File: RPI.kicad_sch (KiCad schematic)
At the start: 24 parts, among them J1 Conn_01x02_Male, J1 GPIO, J2 Conn_02x12, J4 Conn_01x03, Q1 IRF9540N, U1 LM1085-5.0, U2 CAT24C256

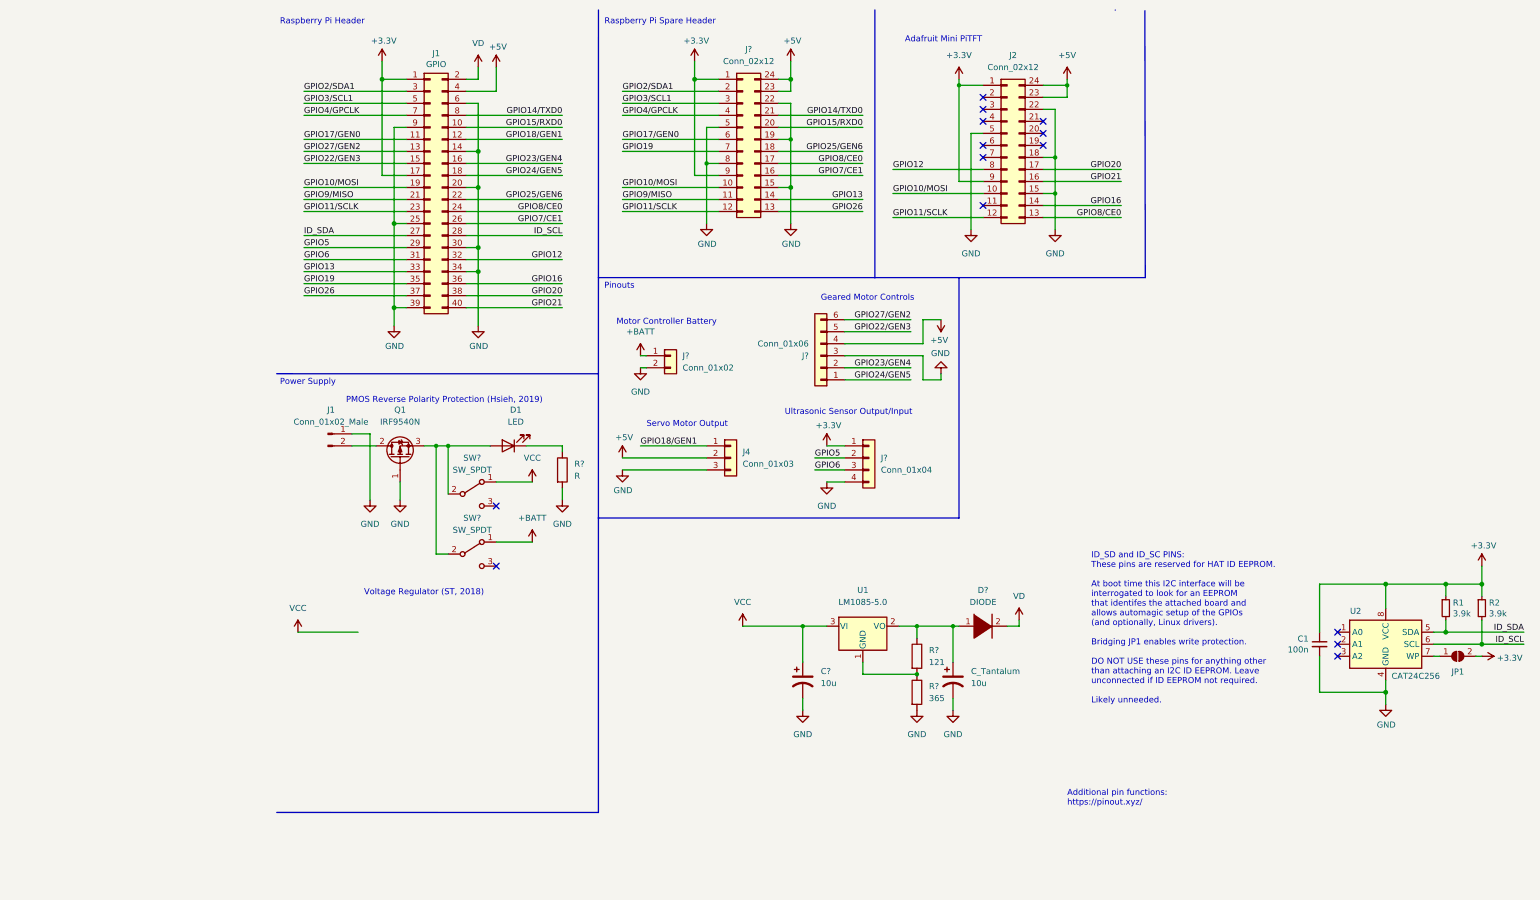
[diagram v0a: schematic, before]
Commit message: Removed EEPROM, Added back power protection
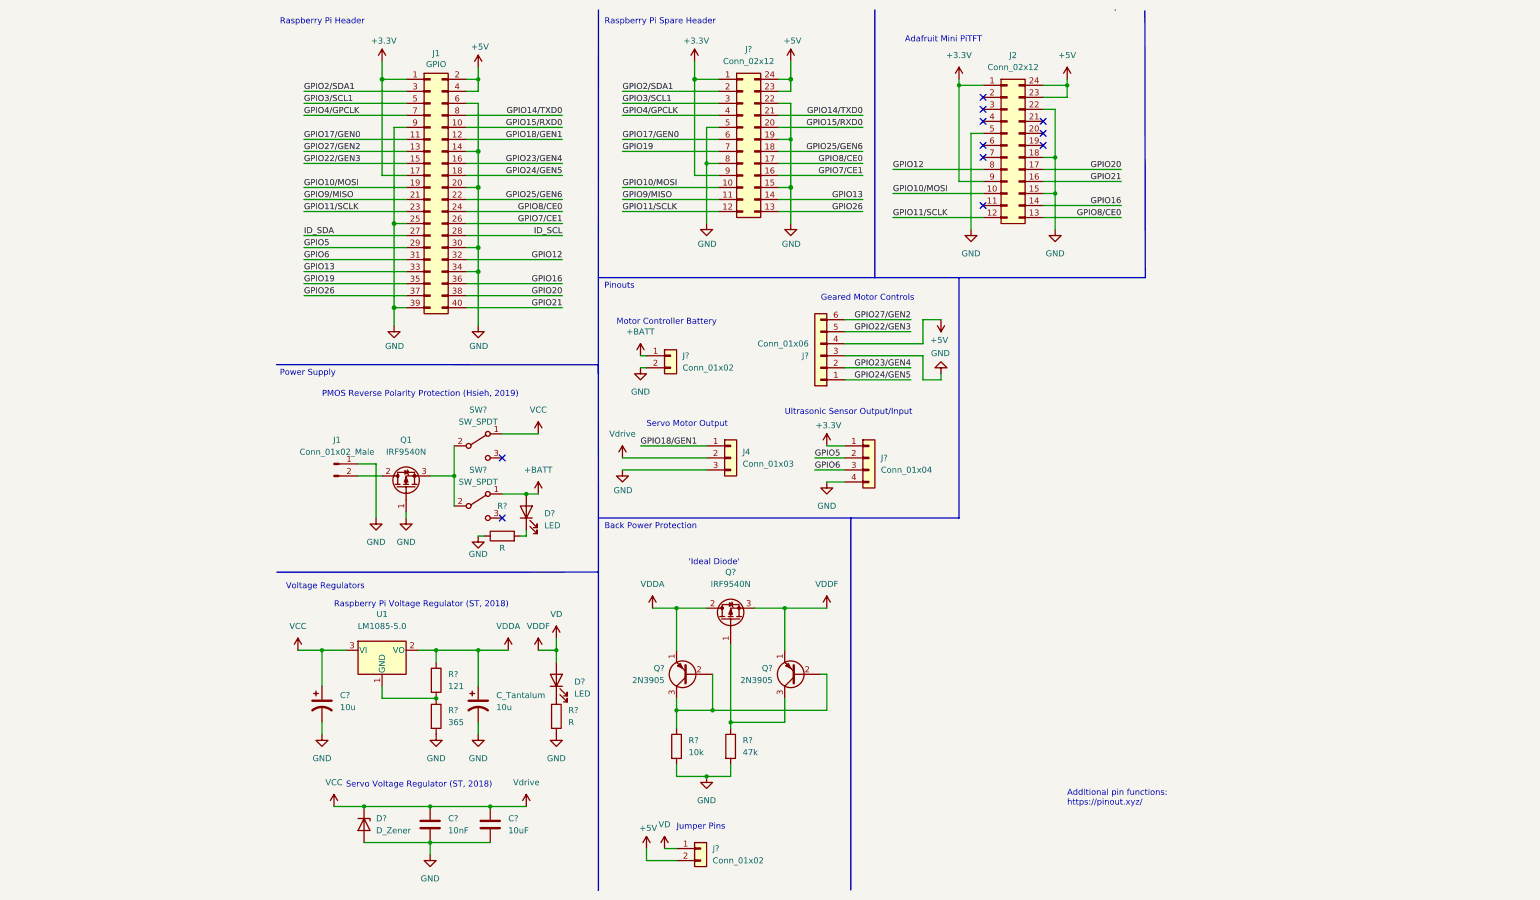
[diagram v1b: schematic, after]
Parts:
- removed C1: 100n, symbol Device:C_Small
- removed D1: LED, symbol Device:LED
- removed D?: DIODE, symbol pspice:DIODE
- removed JP1: ID_WP, symbol Jumper:SolderJumper_2_Open
- removed R1, R2: 3.9k, symbol Device:R_Small
- removed R?: R, symbol Device:R
- removed U2: CAT24C256, symbol Memory_EEPROM:CAT24C256
- added C?: 10uF, symbol Device:C
- added C?: 10nF, symbol Device:C
- added D? (x2): LED, symbol Device:LED
- added D?: D_Zener, symbol Device:D_Zener
- added J?: Conn_01x02, symbol Connector_Generic:Conn_01x02
- added Q? (x2): 2N3905, Package_TO_SOT_THT:TO-92_Inline, symbol Transistor_BJT:2N3905
- added Q?: IRF9540N, Package_TO_SOT_THT:TO-220-3_Vertical, symbol Transistor_FET:IRF9540N
- added R? (x2): R, symbol Device:R
- added R?: 47k, symbol Device:R
- added R?: 10k, symbol Device:R
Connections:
- net +5V: now also J1.2 (Pin_2), J?.2 (Pin_2); no longer J4.2 (Pin_2)
- net +BATT: now also D?.2 (A)
- net GND: now also C?.2, C?.2, D?.2 (A), R?.1, R?.2, R?.2, R?.2
- net VCC: now also J4.2 (Pin_2), C?.1, C?.1, D?.1 (K)
- net VD: now also D?.2 (A), J?.1 (Pin_1), Q?.1 (E), Q?.3 (S); no longer J1.2 (Pin_2)
- net VDDA: now reaches C_Tantalum.1, R?.1, U1.2 (VO)
- net VDDA: now also Q?.1 (E), Q?.2 (D)
- new net: D?.1 (K), R?.1
- new net: Q?.2 (B), Q?.2 (B), Q?.3 (C), R?.1
- new net: D?.1 (K), R?.2
- new net: Q?.1 (G), Q?.3 (C), R?.1
- no-connect marks 14 -> 11
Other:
- note added: "'Ideal Diode'"
- note added: "Back Power Protection"
- note added: "Jumper Pins"
- note added: "Raspberry Pi Voltage Regulator (ST, 2018)"
- note added: "Servo Voltage Regulator (ST, 2018)"
- note added: "Voltage Regulators"
- note removed: "ID_SD and ID_SC PINS: These pins are reserved for HAT ID EEPROM. At boot time this I2C interface will be interrogated to look for an EEPROM that identifes the attached board and allows automagic setup of the GPIOs (and optionally, Linux drivers). Bridging JP1 enables write protection. DO NOT USE these pins for anything other than attaching an I2C ID EEPROM. Leave unconnected if ID EEPROM not requ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"
- note removed: "Voltage Regulator (ST, 2018)"
- moved on the sheet: C?, C_Tantalum, J1, Q1, R?, SW?, U1

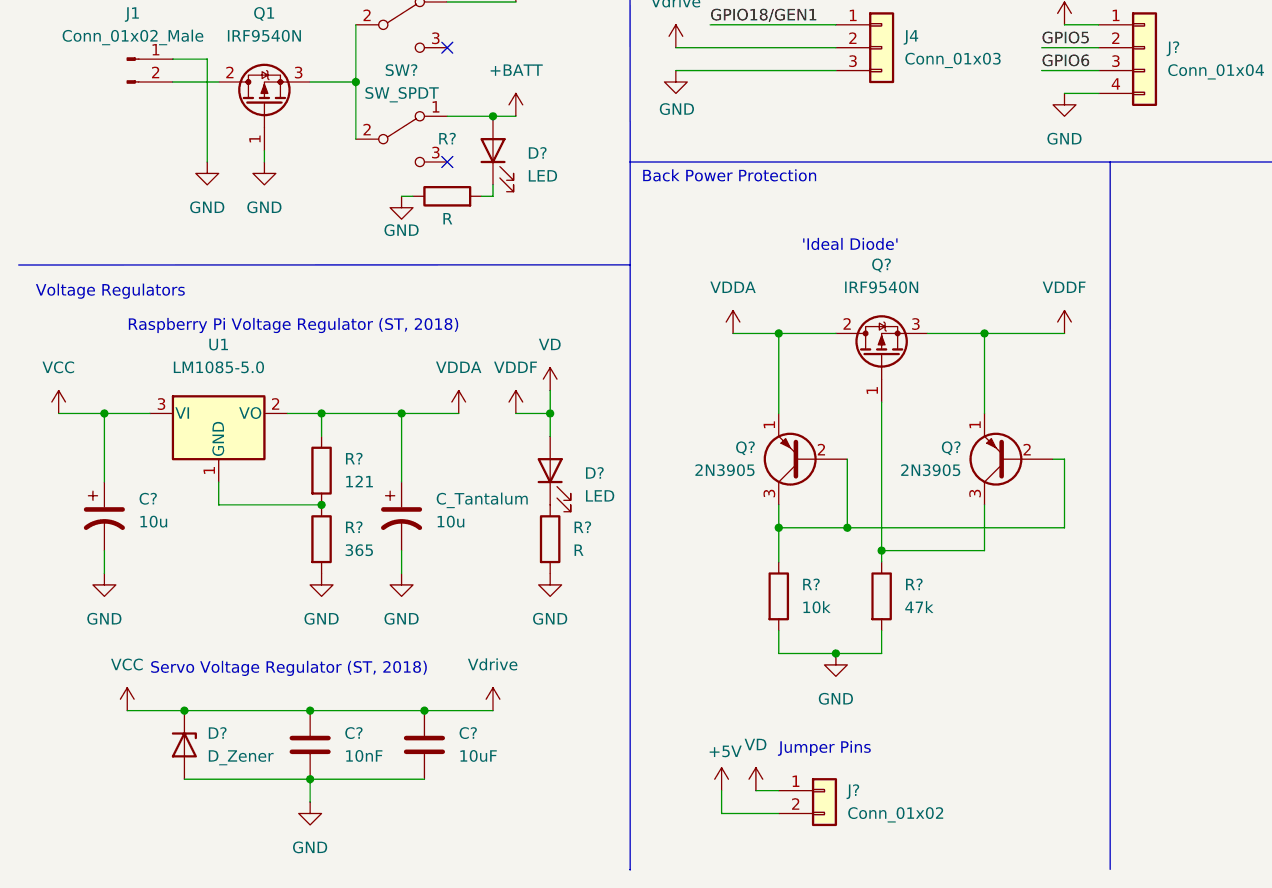
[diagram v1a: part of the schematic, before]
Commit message: Process to update headers for SMDs
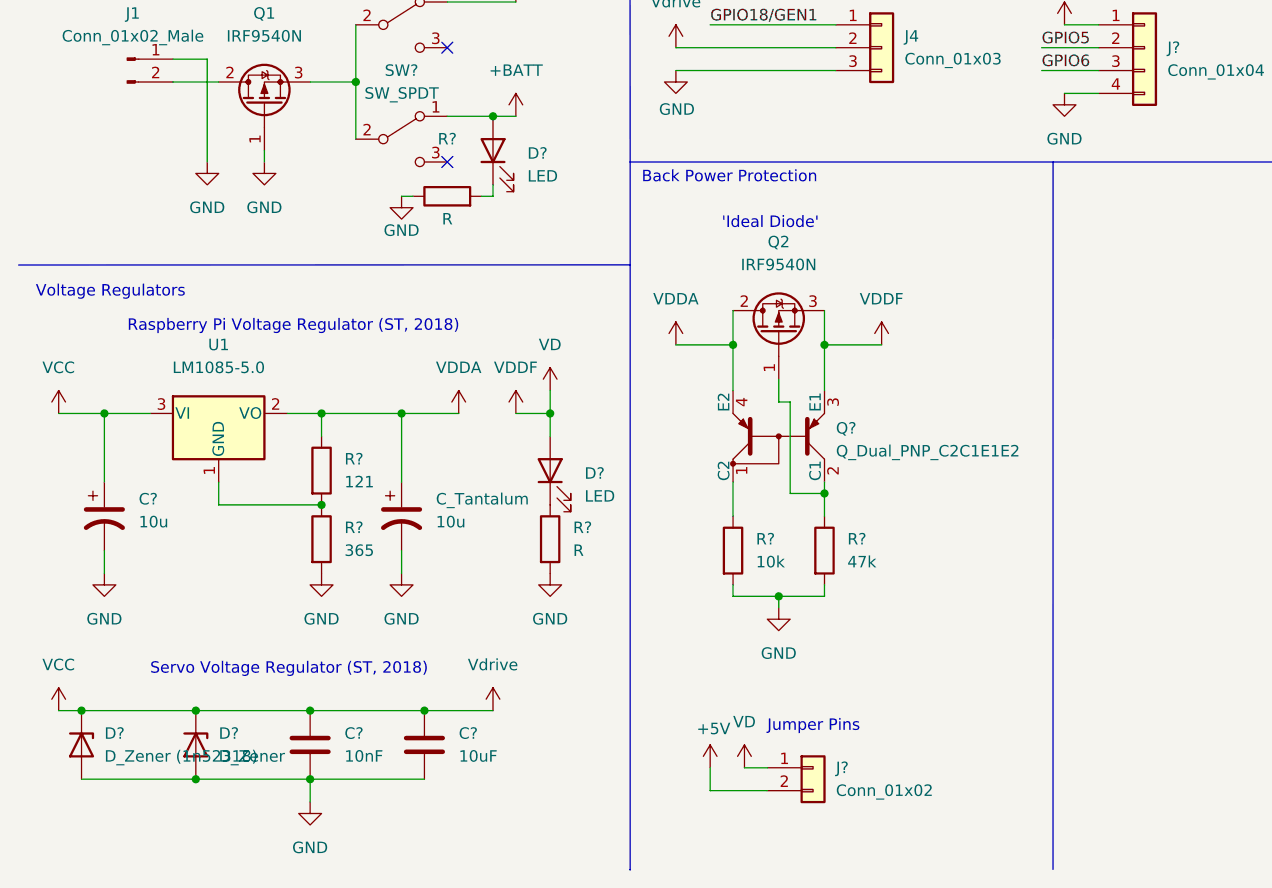
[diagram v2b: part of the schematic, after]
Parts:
- removed Q? (x2): 2N3905, Package_TO_SOT_THT:TO-92_Inline, symbol Transistor_BJT:2N3905
- removed Q?: IRF9540N, Package_TO_SOT_THT:TO-220-3_Vertical, symbol Transistor_FET:IRF9540N
- added D?: D_Zener (1n52318), symbol Device:D_Zener
- added Q2: IRF9540N, Package_TO_SOT_THT:TO-220-3_Vertical, symbol Transistor_FET:IRF9540N
- added Q?: Q_Dual_PNP_C2C1E1E2, symbol Device:Q_Dual_PNP_C2C1E1E2
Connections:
- net GND: now also D?.2 (A)
- net VCC: now also D?.1 (K)
- net VD: now also Q2.3 (S), Q?.3 (E1)
- net VDDA: now also Q2.2 (D), Q?.4 (E2)
- net at R?.1: now also Q?.1 (C2)
- net at R?.1: now also Q2.1 (G), Q?.2 (C1)
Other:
- moved on the sheet: D?, J?, R?

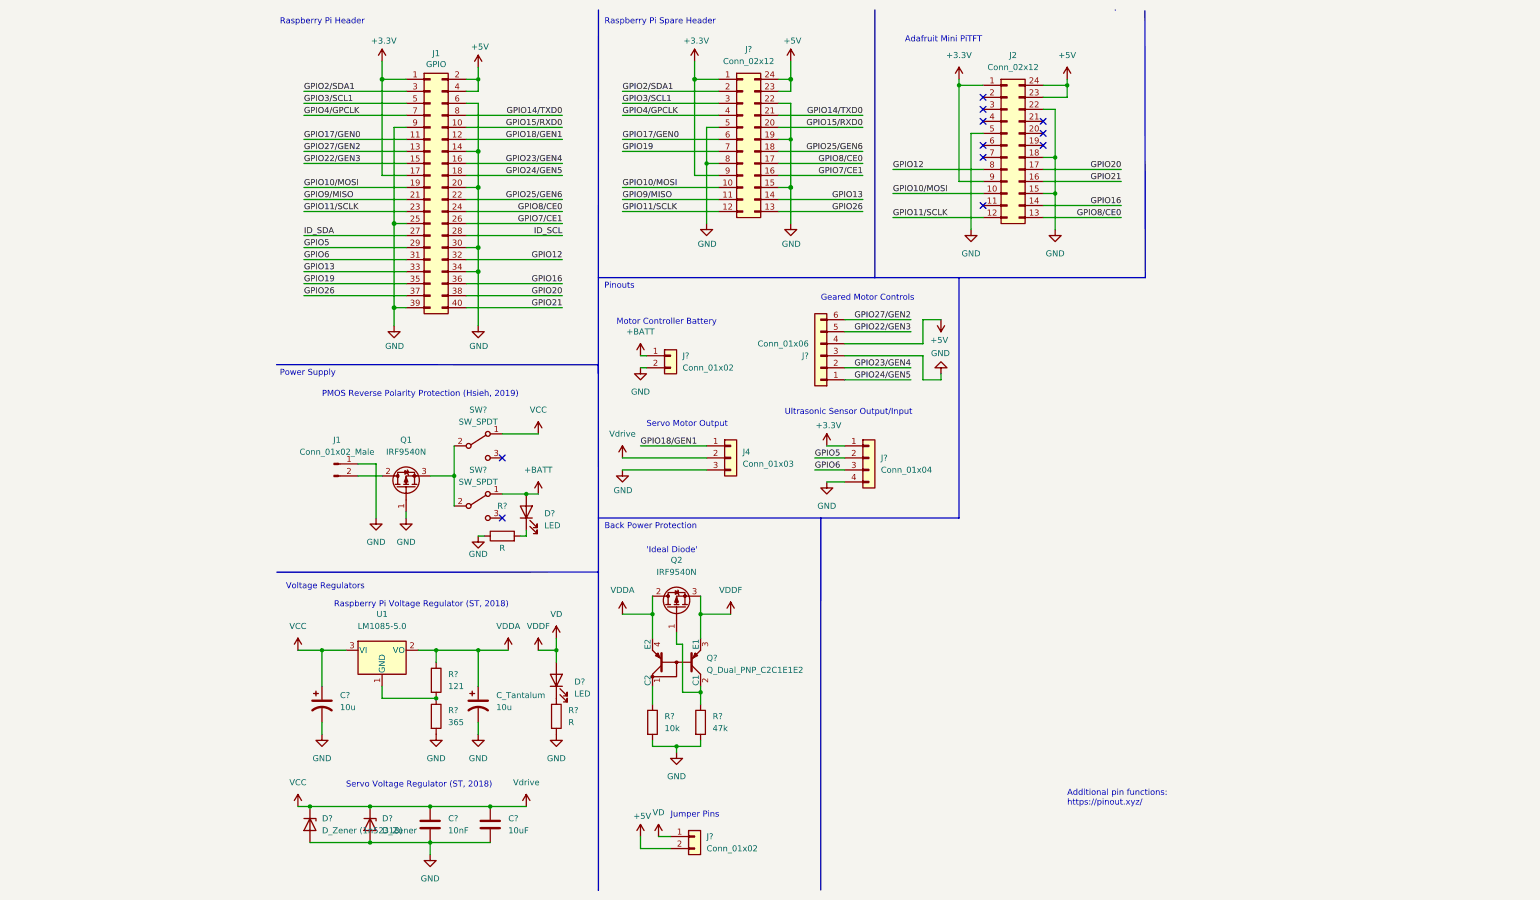
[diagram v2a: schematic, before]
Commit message: Component footprints done - only need cap & sw tbd
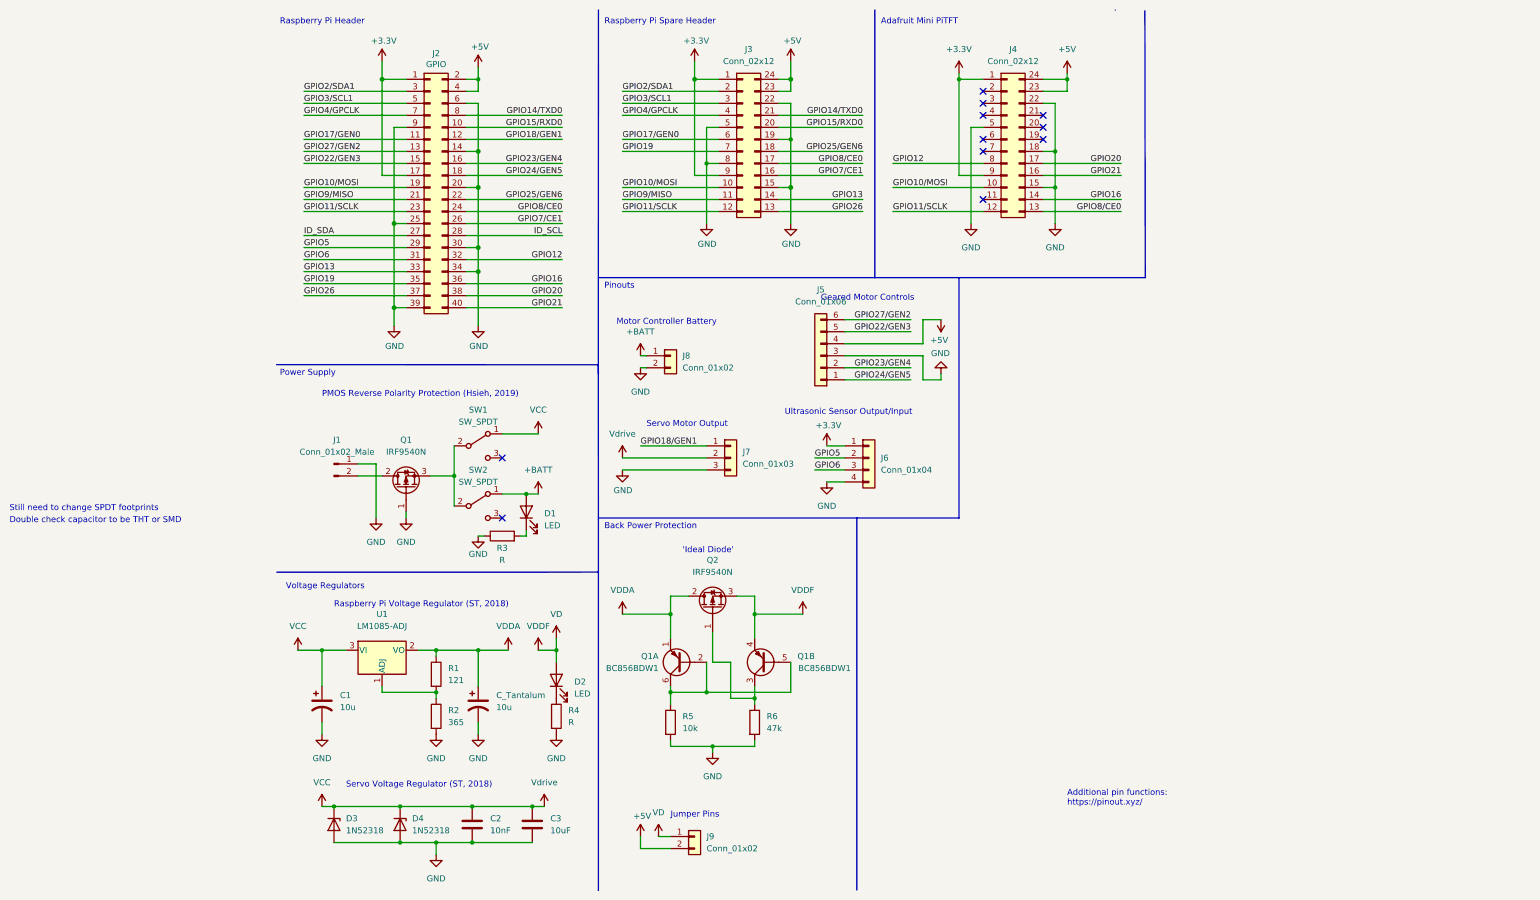
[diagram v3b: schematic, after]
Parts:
- removed D?: D_Zener, symbol Device:D_Zener
- removed Q?: Q_Dual_PNP_C2C1E1E2, symbol Device:Q_Dual_PNP_C2C1E1E2
- removed R? (x2): R, symbol Device:R
- removed R?: 121, symbol Device:R
- removed R?: 365, symbol Device:R
- removed R?: 47k, symbol Device:R
- removed R?: 10k, symbol Device:R
- removed U1: LM1085-5.0, symbol Regulator_Linear:LM1085-5.0
- added D4: 1N52318, Diode_THT:D_DO-35_SOD27_P7.62mm_Horizontal, symbol Device:D_Zener
- added Q1: BC856BDW1, Package_TO_SOT_SMD:SOT-363_SC-70-6, symbol Transistor_BJT:BC856BDW1
- added unit 2 of Q1
- added R1: 121, Resistor_SMD:R_0805_2012Metric_Pad1.20x1.40mm_HandSolder, symbol Device:R
- added R2: 365, Resistor_SMD:R_0805_2012Metric_Pad1.20x1.40mm_HandSolder, symbol Device:R
- added R3, R4: R, Resistor_SMD:R_0805_2012Metric_Pad1.20x1.40mm_HandSolder, symbol Device:R
- added R5: 10k, Resistor_SMD:R_0805_2012Metric_Pad1.20x1.40mm_HandSolder, symbol Device:R
- added R6: 47k, Resistor_SMD:R_0805_2012Metric_Pad1.20x1.40mm_HandSolder, symbol Device:R
- added U1: LM1085-ADJ, symbol Regulator_Linear:LM1085-ADJ
- D1, D2: renamed from D?; footprint (none) -> Diode_SMD:D_0805_2012Metric_Pad1.15x1.40mm_HandSolder
- D3: renamed from D?; value D_Zener (1n52318) -> 1N52318; footprint (none) -> Diode_THT:D_DO-35_SOD27_P7.62mm_Horizontal
- J3: renamed from J?; footprint (none) -> Connector_PinSocket_2.54mm:PinSocket_2x12_P2.54mm_Vertical
- J4: renamed from J2; footprint (none) -> Connector_PinSocket_2.54mm:PinSocket_2x12_P2.54mm_Vertical
- J5: renamed from J?; footprint (none) -> Connector_PinSocket_2.54mm:PinSocket_1x06_P2.54mm_Vertical
- J6: renamed from J?; footprint (none) -> Connector_PinSocket_2.54mm:PinSocket_1x04_P2.54mm_Vertical
- J7: renamed from J4; footprint (none) -> Connector_PinSocket_2.54mm:PinSocket_1x03_P2.54mm_Vertical
- J8, J9: renamed from J?; footprint (none) -> Connector_PinSocket_2.54mm:PinSocket_1x02_P2.54mm_Vertical
- gave numbers to parts that had none: 5
- renumbered J1 to J2
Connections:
- net GND: now also D4.2 (A), R2.2, R3.1, R4.2, R5.2, R6.2
- net VCC: now also D4.1 (K), U1.3 (VI)
- net VD: now also Q1.4 (E2)
- net VDDA: now also Q1.1 (E1), R1.1, U1.2 (VO)
- net at D2.1 (K): now also R4.1
- net at D1.1 (K): now also R3.2
- net at Q2.1 (G): now also Q1.3 (C2), R6.1
- new net: R1.2, R2.1, U1.1 (ADJ)
- new net: Q1.2 (B1), Q1.5 (B2), Q1.6 (C1), R5.1
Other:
- note added: "Double check capacitor to be THT or SMD"
- note added: "Still need to change SPDT footprints"
- moved on the sheet: C2, C3, D3, J4, Q2
